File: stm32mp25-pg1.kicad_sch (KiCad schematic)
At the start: 1 part, among them U1 STM32MP257FAI3

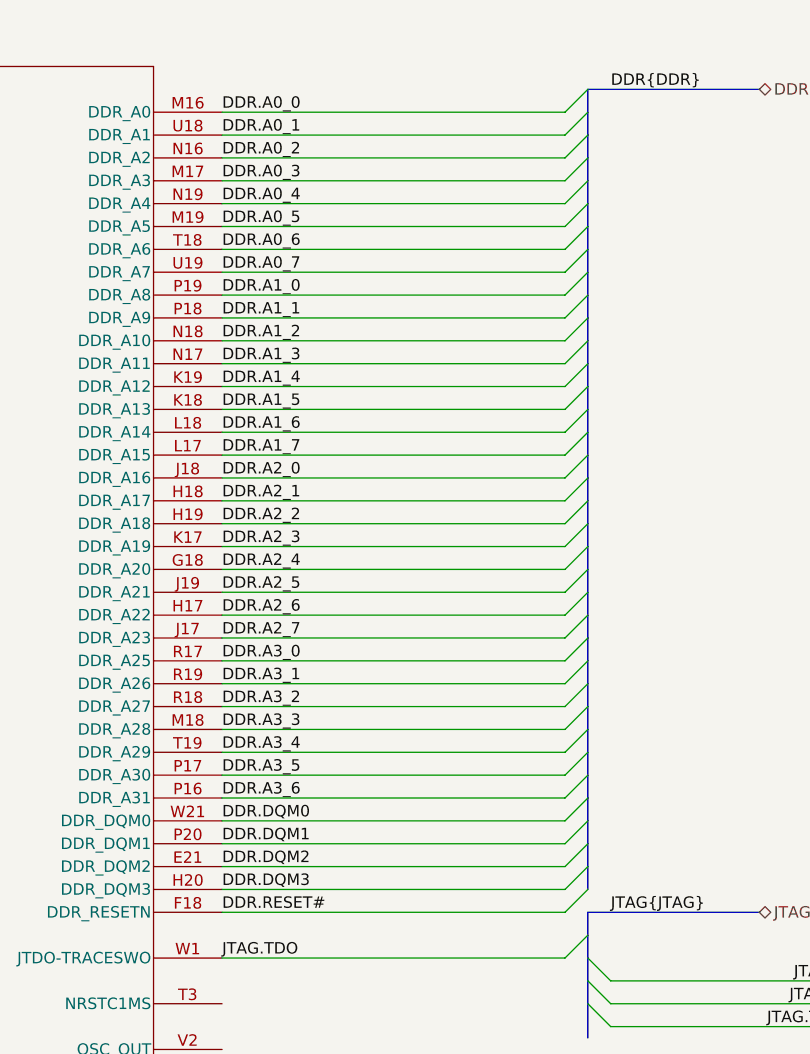
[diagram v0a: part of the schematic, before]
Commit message: connected lpddr4 to mp
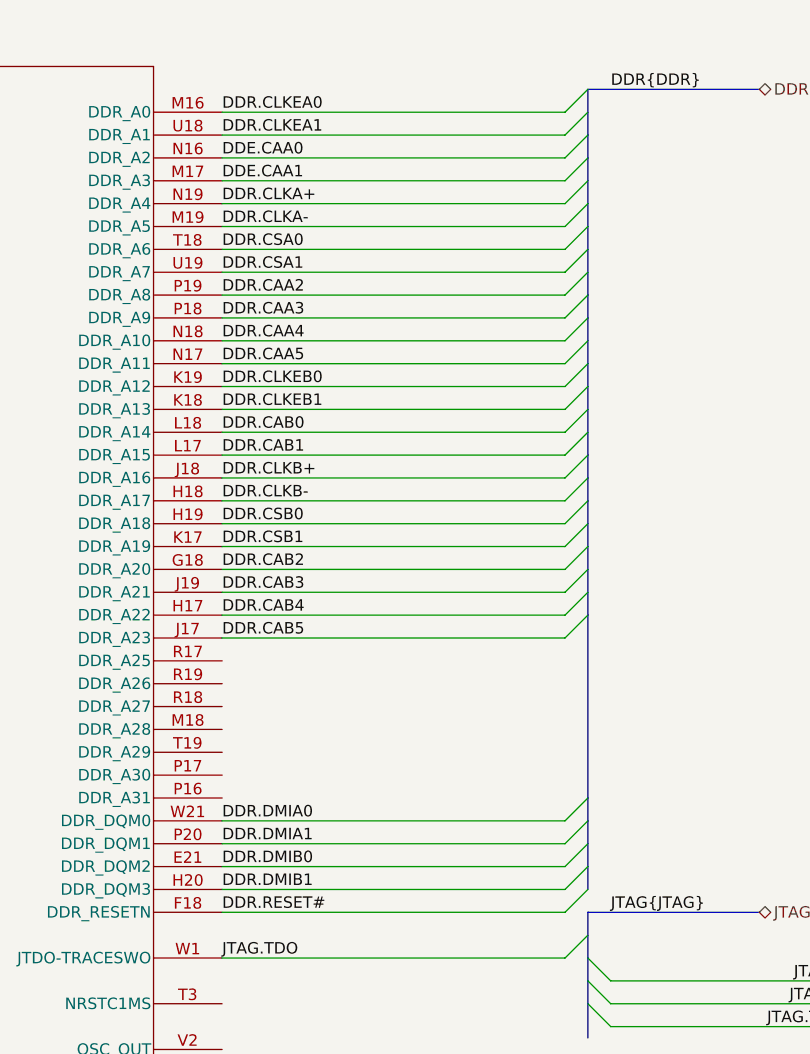
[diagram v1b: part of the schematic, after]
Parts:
- U1: footprint TFBGA436_STM -> STM32MP257FAI3:TFBGA436_STM
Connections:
- net DDR.A0_0 renamed DDR.CLKEA0
- net DDR.A0_1 renamed DDR.CLKEA1
- net DDR.A0_2 renamed DDE.CAA0
- net DDR.A0_3 renamed DDE.CAA1
- net DDR.A0_4 renamed DDR.CLKA+
- net DDR.A0_5 renamed DDR.CLKA-
- net DDR.A0_6 renamed DDR.CSA0
- net DDR.A0_7 renamed DDR.CSA1
- net DDR.A1_0 renamed DDR.CAA2
- net DDR.A1_1 renamed DDR.CAA3
- net DDR.A1_2 renamed DDR.CAA4
- net DDR.A1_3 renamed DDR.CAA5
- net DDR.A1_4 renamed DDR.CLKEB0
- net DDR.A1_5 renamed DDR.CLKEB1
- net DDR.A1_6 renamed DDR.CAB0
- net DDR.A1_7 renamed DDR.CAB1
- net DDR.A2_0 renamed DDR.CLKB+
- net DDR.A2_1 renamed DDR.CLKB-
- net DDR.A2_2 renamed DDR.CSB0
- net DDR.A2_3 renamed DDR.CSB1
- net DDR.A2_4 renamed DDR.CAB2
- net DDR.A2_5 renamed DDR.CAB3
- net DDR.A2_6 renamed DDR.CAB4
- net DDR.A2_7 renamed DDR.CAB5
- net DDR.A3_0: no longer names the net of U1.R17 (DDR_A25)
- net DDR.A3_1: no longer names the net of U1.R19 (DDR_A26)
- net DDR.A3_2: no longer names the net of U1.R18 (DDR_A27)
- net DDR.A3_3: no longer names the net of U1.M18 (DDR_A28)
- net DDR.A3_4: no longer names the net of U1.T19 (DDR_A29)
- net DDR.A3_5: no longer names the net of U1.P17 (DDR_A30)
- net DDR.A3_6: no longer names the net of U1.P16 (DDR_A31)
- net DDR.DQM0 renamed DDR.DMIA0
- net DDR.DQM1 renamed DDR.DMIA1
- net DDR.DQM2 renamed DDR.DMIB0
- net DDR.DQM3 renamed DDR.DMIB1
